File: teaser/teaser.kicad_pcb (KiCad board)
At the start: 2 copper layers, 43 x 115 mm, 67 parts, among them J1 Programator, J2 AC_Plug, J3 OLED, J4 battery, Q1 MMBTA44, Q2 MMBTA44, Q3 MMBTA44, Q4 MMBTA44, Q6 AO3401A, SW1 Włancznik, SW7 SW_Push, U2 LM1117MP-5.0, U3 ATmega328P-A, Y1 16kHz

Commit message: Sorted some silkscreen annotations
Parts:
- moved D10 73.5 mm to (148.8, 82.4)
- moved D11 73.5 mm to (144.3, 82.4)
- moved D5 73.5 mm to (156.3, 99.6)
- moved D7 73.5 mm to (146.3, 106.9)
- moved D9 73.5 mm to (139.8, 82.4)
- moved R1 73.5 mm to (142.6, 87.4)
- moved R11 73.5 mm to (128.8, 78.7)
- moved R2 73.5 mm to (151.1, 83.4)
- moved R3 73.5 mm to (148.1, 87.4)
- moved R4 73.5 mm to (142.1, 83.4)
- moved R5 73.5 mm to (145.3, 87.4)
- moved R6 73.5 mm to (146.6, 83.4)
- moved R8 73.5 mm to (133.8, 78.7)
- moved SW1 73.5 mm to (140.6, 74.2)
- moved U2 73.5 mm to (147.7, 67.3)
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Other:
- board text added: "+ -"
- board text added: "C13"
- board text added: "CH1"
- board text added: "CH2"
- board text added: "CH3"
- board text added: "Designed by Mateusz Majewski"
- board text added: "MEASURE"
- board text added: "SCL"
- board text added: "SDA"

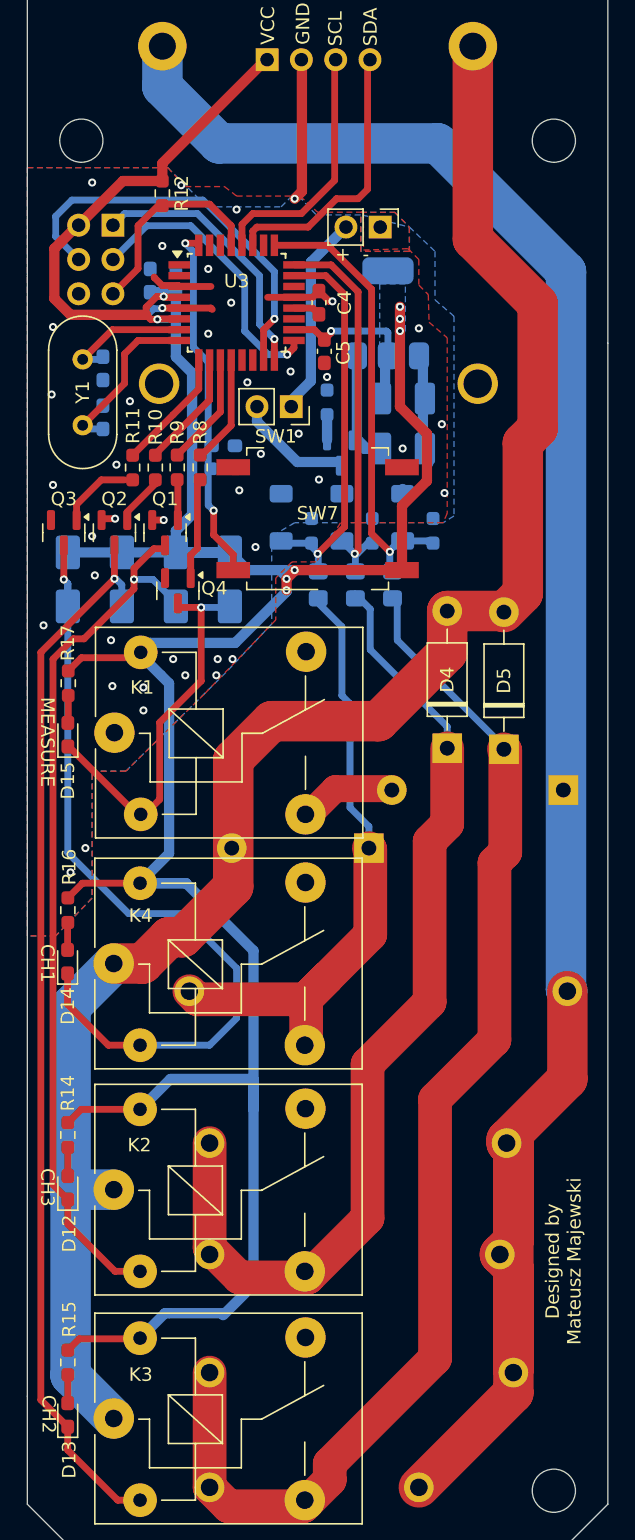
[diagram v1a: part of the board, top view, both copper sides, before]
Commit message: Finished layout, silkscreen and generated gerbers
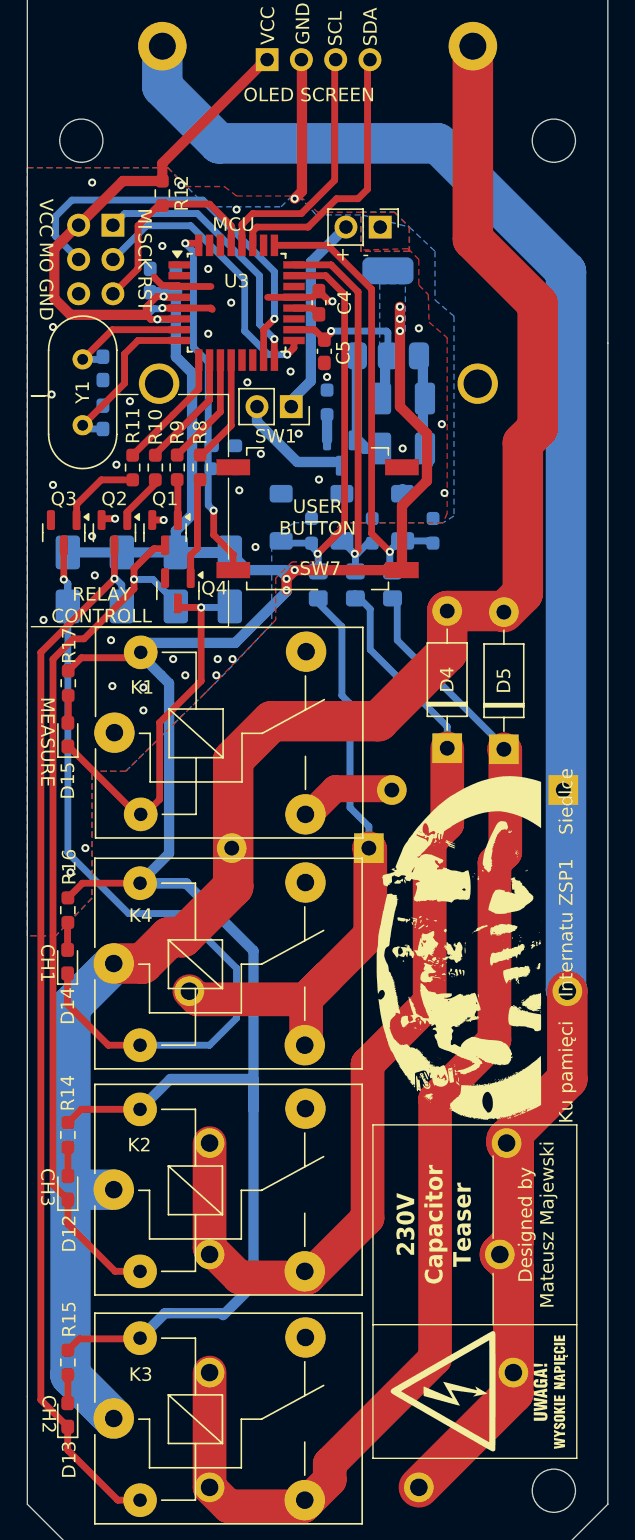
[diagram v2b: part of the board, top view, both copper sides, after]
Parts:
- added G***: LOGO, LOGO, F.Cu at (151.9, 116.0)
- added G***: LOGO, LOGO, F.Cu at (154.7, 147.2)
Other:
- board text added: "150n"
- board text added: "1u"
- board text added: "230V Capacitor Teaser"
- board text added: "330n"
- board text added: "680n"
- board text added: "Ku pamięci Internatu ZSP1 Siedlce"
- board text added: "MCU"
- board text added: "OLED SCREEN"
- board text added: "POWER MANAGEMENT"
- board text added: "RELAY CONTROLL"
- board text added: "USER BUTTON"
- board text added: "VOLTAGE MEASUREMENT"
